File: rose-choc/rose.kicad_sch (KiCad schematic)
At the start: 67 parts, among them SW1 Switch, U1 Arduino_Pro_Micro, U2 TRRS

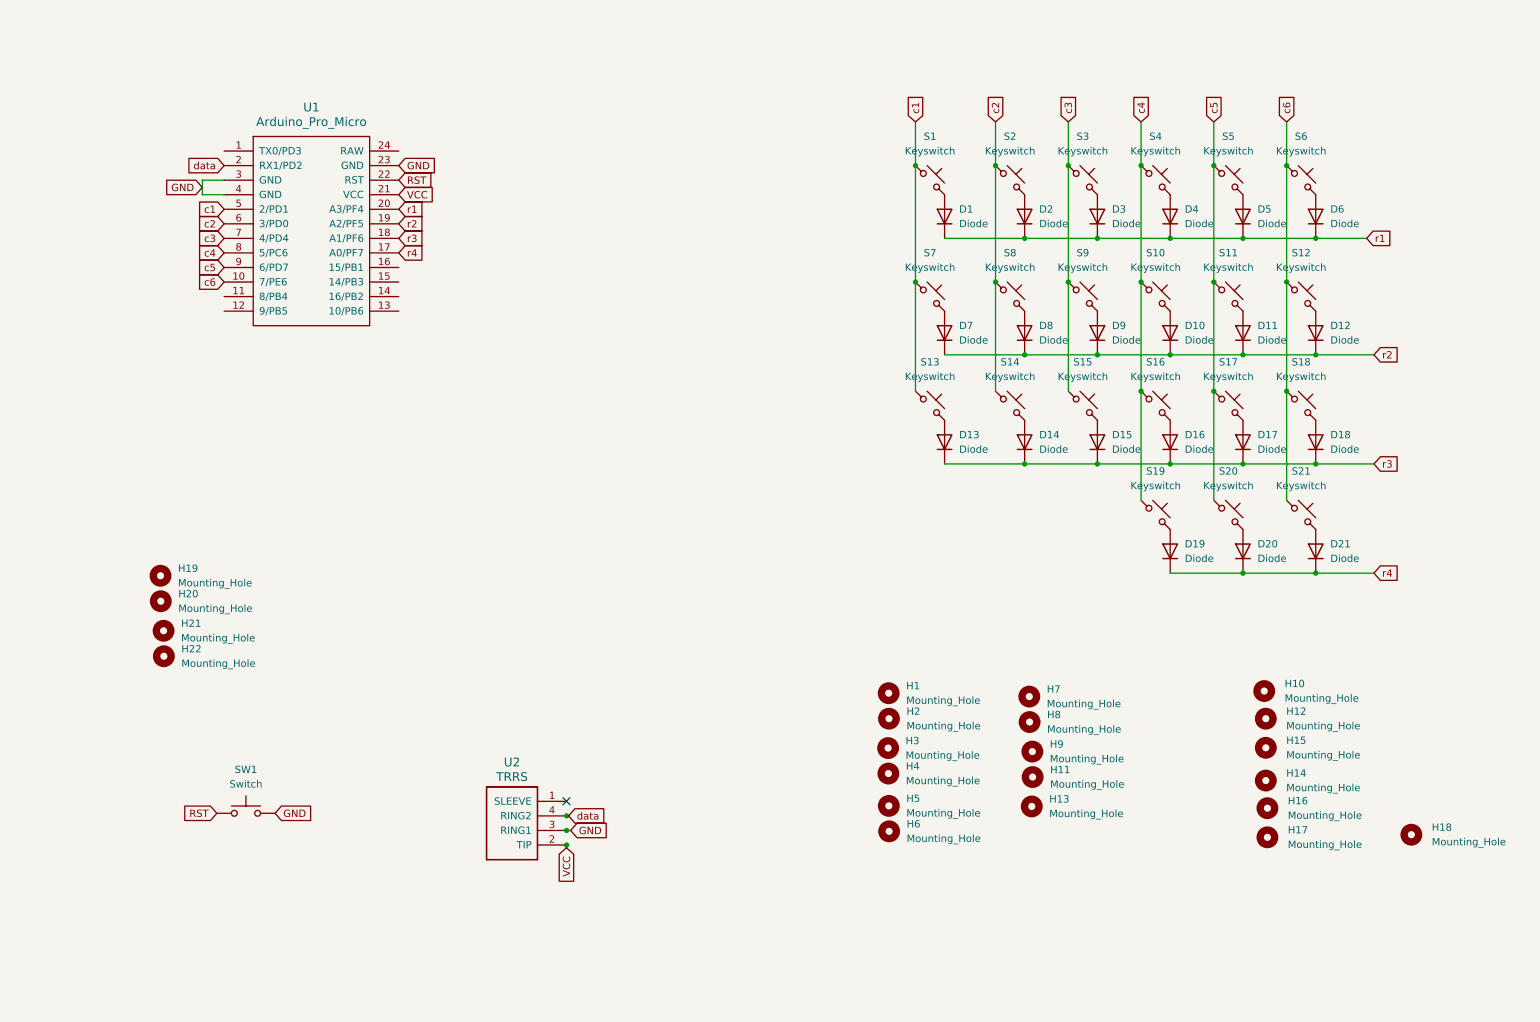
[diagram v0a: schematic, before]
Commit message: improve tracks and fix vias
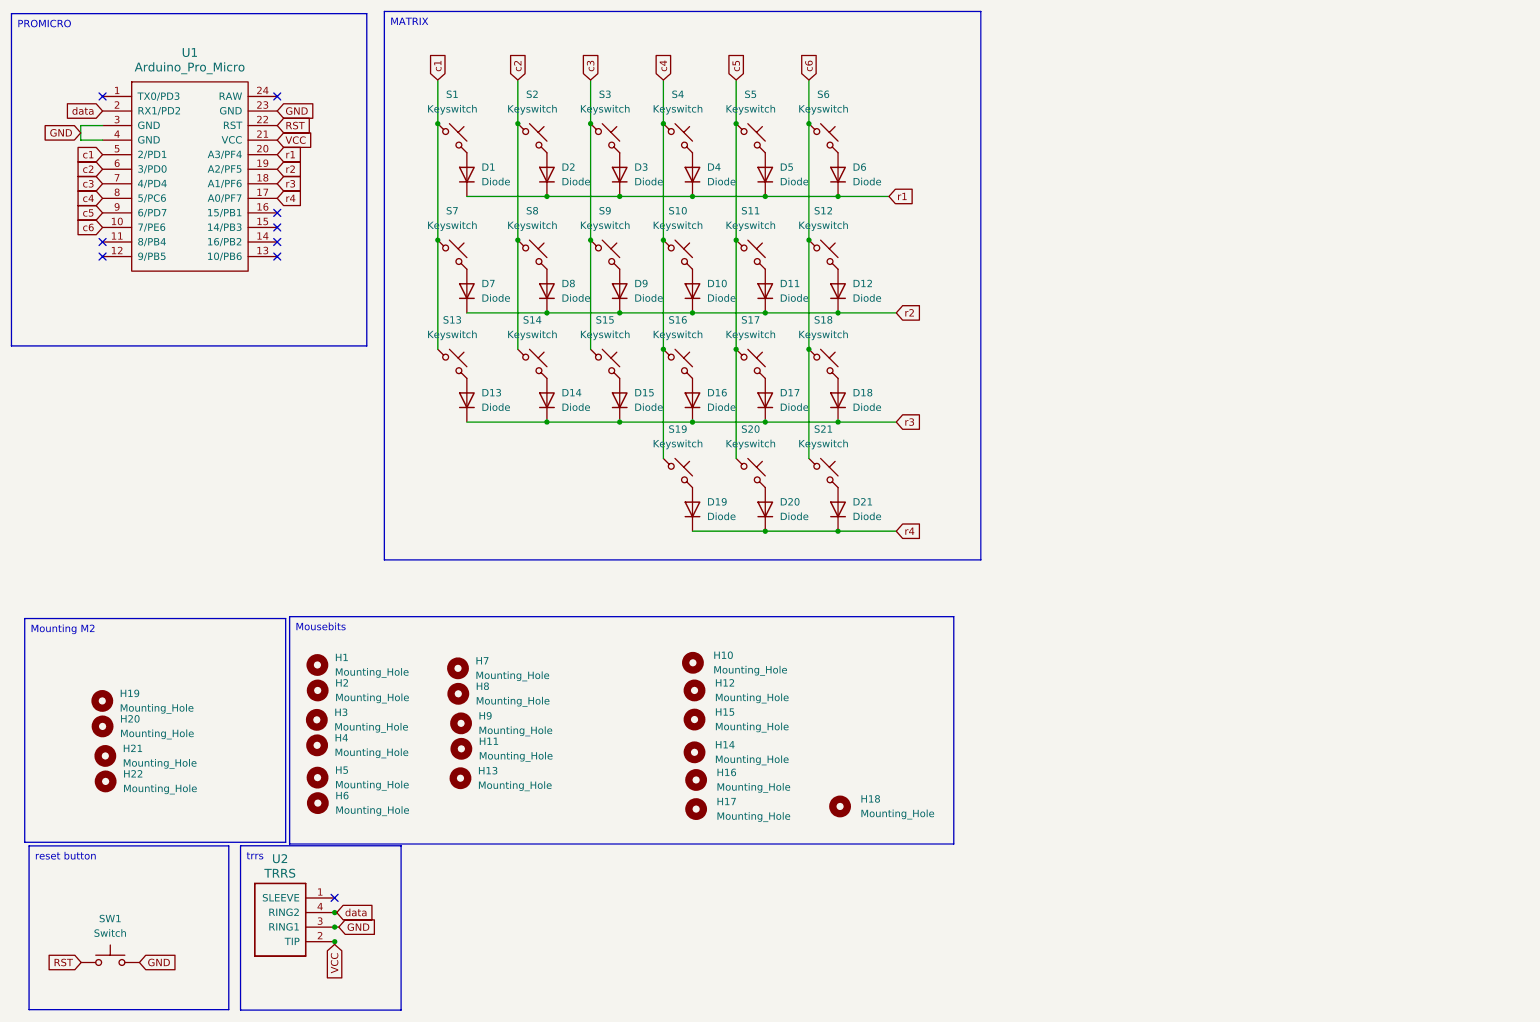
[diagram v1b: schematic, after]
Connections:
- no-connect marks 1 -> 9
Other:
- moved on the sheet: D1, D10, D11, D12, D13, D14, D15, D16, D17, D18, D19, D2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

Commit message: change diode footprint
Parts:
- D1, D10, D11, D12, D13, D14, D15, D16, D17, D18, D19, D2, D20, D21, D3, D4, D5, D6, D7, D8, D9: footprint kbd:D3_SMD -> swoop:D3_SMD
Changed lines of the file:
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@@
       (effects (font (size 1.27 1.27)) (justify right))
     )
-    (property "Footprint" "kbd:D3_SMD" (at 163.0172 81.5848 0)
+    (property "Footprint" "swoop:D3_SMD" (at 163.0172 81.5848 0)
       (effects (font (size 1.27 1.27)) hide)
     )
@@
       (effects (font (size 1.27 1.27)) (justify right))
     )
-    (property "Footprint" "kbd:D3_SMD" (at 112.2172 62.5348 0)
+    (property "Footprint" "swoop:D3_SMD" (at 112.2172 62.5348 0)
       (effects (font (size 1.27 1.27)) hide)
     )
@@
       (effects (font (size 1.27 1.27)) (justify right))
     )
-    (property "Footprint" "kbd:D3_SMD" (at 150.3172 42.2148 0)
+    (property "Footprint" "swoop:D3_SMD" (at 150.3172 42.2148 0)
       (effects (font (size 1.27 1.27)) hide)
     )
@@
       (effects (font (size 1.27 1.27)) (justify right))
     )
-    (property "Footprint" "kbd:D3_SMD" (at 124.9172 42.2148 0)
+    (property "Footprint" "swoop:D3_SMD" (at 124.9172 42.2148 0)
       (effects (font (size 1.27 1.27)) hide)
     )
@@
       (effects (font (size 1.27 1.27)) (justify right))
     )
-    (property "Footprint" "kbd:D3_SMD" (at 137.6172 100.6348 0)
+    (property "Footprint" "swoop:D3_SMD" (at 137.6172 100.6348 0)
       (effects (font (size 1.27 1.27)) hide)
     )
@@
       (effects (font (size 1.27 1.27)) (justify right))
     )
-    (property "Footprint" "kbd:D3_SMD" (at 98.2472 81.5848 0)
+    (property "Footprint" "swoop:D3_SMD" (at 98.2472 81.5848 0)
       (effects (font (size 1.27 1.27)) hide)
     )
@@
       (effects (font (size 1.27 1.27)) (justify right))
     )
-    (property "Footprint" "kbd:D3_SMD" (at 137.6172 42.2148 0)
+    (property "Footprint" "swoop:D3_SMD" (at 137.6172 42.2148 0)
       (effects (font (size 1.27 1.27)) hide)
     )
@@
       (effects (font (size 1.27 1.27)) (justify right))
     )
-    (property "Footprint" "kbd:D3_SMD" (at 112.2172 81.5848 0)
+    (property "Footprint" "swoop:D3_SMD" (at 112.2172 81.5848 0)
       (effects (font (size 1.27 1.27)) hide)
     )
@@
       (effects (font (size 1.27 1.27)) (justify right))
     )
-    (property "Footprint" "kbd:D3_SMD" (at 150.3172 100.6348 0)
+    (property "Footprint" "swoop:D3_SMD" (at 150.3172 100.6348 0)
       (effects (font (size 1.27 1.27)) hide)
     )
@@
       (effects (font (size 1.27 1.27)) (justify right))
     )
-    (property "Footprint" "kbd:D3_SMD" (at 112.2172 42.2148 0)
+    (property "Footprint" "swoop:D3_SMD" (at 112.2172 42.2148 0)
       (effects (font (size 1.27 1.27)) hide)
     )
@@
       (effects (font (size 1.27 1.27)) (justify right))
     )
-    (property "Footprint" "kbd:D3_SMD" (at 150.3172 81.5848 0)
+    (property "Footprint" "swoop:D3_SMD" (at 150.3172 81.5848 0)
       (effects (font (size 1.27 1.27)) hide)
     )
@@
       (effects (font (size 1.27 1.27)) (justify right))
     )
-    (property "Footprint" "kbd:D3_SMD" (at 98.2472 42.2148 0)
+    (property "Footprint" "swoop:D3_SMD" (at 98.2472 42.2148 0)
       (effects (font (size 1.27 1.27)) hide)
     )
@@
       (effects (font (size 1.27 1.27)) (justify right))
     )
-    (property "Footprint" "kbd:D3_SMD" (at 137.6172 62.5348 0)
+    (property "Footprint" "swoop:D3_SMD" (at 137.6172 62.5348 0)
       (effects (font (size 1.27 1.27)) hide)
     )
@@
       (effects (font (size 1.27 1.27)) (justify right))
     )
-    (property "Footprint" "kbd:D3_SMD" (at 163.0172 42.2148 0)
+    (property "Footprint" "swoop:D3_SMD" (at 163.0172 42.2148 0)
       (effects (font (size 1.27 1.27)) hide)
     )
@@
       (effects (font (size 1.27 1.27)) (justify right))
     )
-    (property "Footprint" "kbd:D3_SMD" (at 137.6172 81.5848 0)
+    (property "Footprint" "swoop:D3_SMD" (at 137.6172 81.5848 0)
       (effects (font (size 1.27 1.27)) hide)
     )
@@
       (effects (font (size 1.27 1.27)) (justify right))
     )
-    (property "Footprint" "kbd:D3_SMD" (at 124.9172 62.5348 0)
+    (property "Footprint" "swoop:D3_SMD" (at 124.9172 62.5348 0)
       (effects (font (size 1.27 1.27)) hide)
     )
@@
       (effects (font (size 1.27 1.27)) (justify right))
     )
-    (property "Footprint" "kbd:D3_SMD" (at 163.0172 100.6348 0)
+    (property "Footprint" "swoop:D3_SMD" (at 163.0172 100.6348 0)
       (effects (font (size 1.27 1.27)) hide)
     )
@@
       (effects (font (size 1.27 1.27)) (justify right))
     )
-    (property "Footprint" "kbd:D3_SMD" (at 163.0172 62.5348 0)
+    (property "Footprint" "swoop:D3_SMD" (at 163.0172 62.5348 0)
       (effects (font (size 1.27 1.27)) hide)
     )
@@
       (effects (font (size 1.27 1.27)) (justify right))
     )
-    (property "Footprint" "kbd:D3_SMD" (at 98.2472 62.5348 0)
+    (property "Footprint" "swoop:D3_SMD" (at 98.2472 62.5348 0)
       (effects (font (size 1.27 1.27)) hide)
     )
@@
       (effects (font (size 1.27 1.27)) (justify right))
     )
-    (property "Footprint" "kbd:D3_SMD" (at 124.9172 81.5848 0)
+    (property "Footprint" "swoop:D3_SMD" (at 124.9172 81.5848 0)
       (effects (font (size 1.27 1.27)) hide)
     )
@@
       (effects (font (size 1.27 1.27)) (justify right))
     )
-    (property "Footprint" "kbd:D3_SMD" (at 150.3172 62.5348 0)
-      (effects (font (size 1.27 1.27)) hide)
-    )
+    (property "Footprint" "swoop:D3_SMD" (at 150.3172 62.5348 0)
+      (effects (font (size 1.27 1.27)) hide)
+    )
